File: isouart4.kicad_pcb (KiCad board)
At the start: 2 copper layers, 89 x 99 mm, 83 parts, among them J1 USB_B, J2 Conn_01x04, J3 Conn_01x04, J4 Conn_01x04, J5 Conn_01x04, U1 AMS1117-3.3, U10 74HC123, U11 74HC123, U2 π122U31, U3 π122U31, U4 π122U31, U5 π122U31, U7 CH344Q, U8 74HC123, U9 74HC123, Y1 8MHz

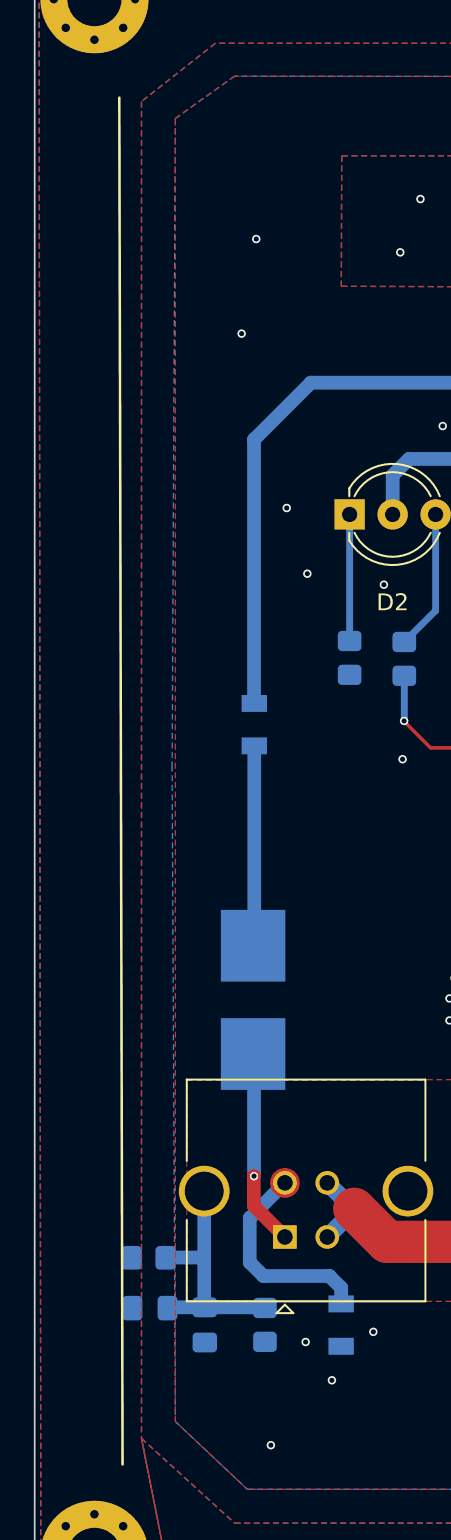
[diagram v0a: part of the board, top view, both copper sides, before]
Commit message: Adjust R1, C1 and C10 poisitions
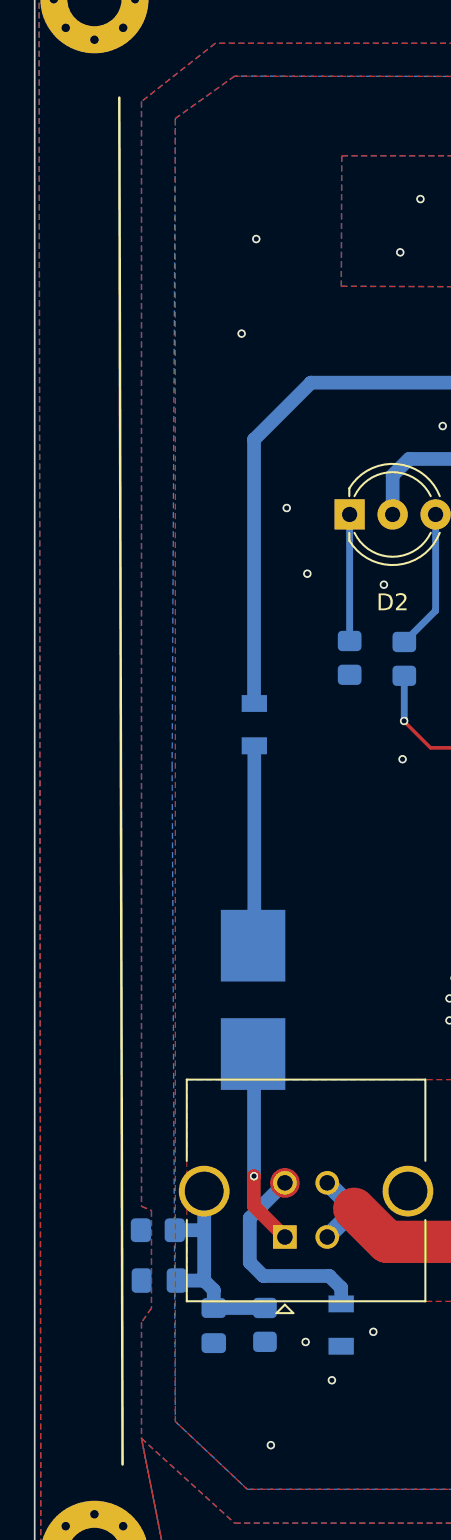
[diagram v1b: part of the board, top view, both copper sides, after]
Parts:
- moved R1 1.72 mm to (147.0, 115.7)
- moved C3 1.72 mm to (147.0, 118.7)
- moved C10 0.53 mm to (150.3, 121.3)
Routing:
- net /USBSHLD: track 14.9 -> 13.6 mm
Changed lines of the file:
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@@
   )
   (footprint "Resistor_SMD:R_0805_2012Metric_Pad1.20x1.40mm_HandSolder" (layer "B.Cu")
-    (at 146.425 117.325)
+    (at 146.965 115.695)
     (descr "Resistor SMD 0805 (2012 Metric), square (rectangular) end terminal, IPC_7351 nominal with elongated pad for handsoldering. (Body size source: IPC-SM-782 page 72, https://www.pcb-3d.com/wordpress/wp-content/uploads/ipc-sm-782a_amendment_1_and_2.pdf), generated with kicad-footprint-generator")
     (tags "resistor handsolder")
@@
   )
   (footprint "Capacitor_SMD:C_0805_2012Metric_Pad1.18x1.45mm_HandSolder" (layer "B.Cu")
-    (at 146.5 120.3)
+    (at 147.04 118.67)
     (descr "Capacitor SMD 0805 (2012 Metric), square (rectangular) end terminal, IPC_7351 nominal with elongated pad for handsoldering. (Body size source: IPC-SM-782 page 76, https://www.pcb-3d.com/wordpress/wp-content/uploads/ipc-sm-782a_amendment_1_and_2.pdf, https://docs.google.com/spreadsheets/d/1BsfQQcO9C6DZCsRaXUlFlo91Tg2WpOkGARC1WS5S8t0/edit?usp=sharing), generated with kicad-footprint-generator")
     (tags "capacitor handsolder")
@@
   )
   (footprint "Capacitor_SMD:C_0805_2012Metric_Pad1.18x1.45mm_HandSolder" (layer "B.Cu")
-    (at 149.74 121.29 90)
+    (at 150.27 121.33 90)
     (descr "Capacitor SMD 0805 (2012 Metric), square (rectangular) end terminal, IPC_7351 nominal with elongated pad for handsoldering. (Body size source: IPC-SM-782 page 76, https://www.pcb-3d.com/wordpress/wp-content/uploads/ipc-sm-782a_amendment_1_and_2.pdf, https://docs.google.com/spreadsheets/d/1BsfQQcO9C6DZCsRaXUlFlo91Tg2WpOkGARC1WS5S8t0/edit?usp=sharing), generated with kicad-footprint-generator")
     (tags "capacitor handsolder")
@@
   (segment (start 170.01 110.015) (end 173.665559 106.359441) (width 0.254) (layer "B.Cu") (net 6))
   (segment (start 173.665559 103.543629) (end 173.665559 102.951687) (width 0.254) (layer "B.Cu") (net 6))
-  (segment (start 147.44 117.31) (end 149.70505 117.31) (width 0.8128) (layer "B.Cu") (net 7))
-  (segment (start 149.70505 113.38485) (end 149.70505 117.31) (width 0.8128) (layer "B.Cu") (net 7))
+  (segment (start 149.70505 113.38485) (end 149.70505 115.7) (width 0.8128) (layer "B.Cu") (net 7))
   (segment (start 149.70505 120.21755) (end 149.74 120.2525) (width 0.2) (layer "B.Cu") (net 7))
   (segment (start 153.2585 120.2525) (end 153.296 120.29) (width 0.8128) (layer "B.Cu") (net 7))
-  (segment (start 149.70505 117.31) (end 149.70505 120.21755) (width 0.8128) (layer "B.Cu") (net 7))
-  (segment (start 149.74 120.2525) (end 153.2585 120.2525) (width 0.8128) (layer "B.Cu") (net 7))
-  (segment (start 147.425 117.325) (end 147.44 117.31) (width 0.8128) (layer "B.Cu") (net 7))
-  (segment (start 149.74 120.2525) (end 147.5525 120.2525) (width 0.8128) (layer "B.Cu") (net 7))
+  (segment (start 148.0775 118.67) (end 149.70505 118.67) (width 0.8128) (layer "B.Cu") (net 7))
+  (segment (start 147.965 115.695) (end 149.70005 115.695) (width 0.8128) (layer "B.Cu") (net 7))
+  (segment (start 153.2935 120.2925) (end 153.296 120.29) (width 0.2) (layer "B.Cu") (net 7))
+  (segment (start 150.27 119.23495) (end 149.70505 118.67) (width 0.8128) (layer "B.Cu") (net 7))
+  (segment (start 150.27 120.2925) (end 153.2935 120.2925) (width 0.8128) (layer "B.Cu") (net 7))
+  (segment (start 150.27 120.2925) (end 150.27 119.23495) (width 0.8128) (layer "B.Cu") (net 7))
+  (segment (start 149.70505 115.7) (end 149.70505 118.67) (width 0.8128) (layer "B.Cu") (net 7))
   (segment (start 152.65 84.555) (end 152.665 84.57) (width 0.8128) (layer "B.Cu") (net 8))
   (segment (start 152.65 68.975) (end 152.65 84.555) (width 0.8128) (layer "B.Cu") (net 8))
@@
         (xy 150.36 45.56)
         (xy 146 49)
+        (xy 146 114.28)
+        (xy 146.59 114.53)
+        (xy 146.59 120.3)
+        (xy 146 121.14)
         (xy 146 128)
         (xy 148 138.1)

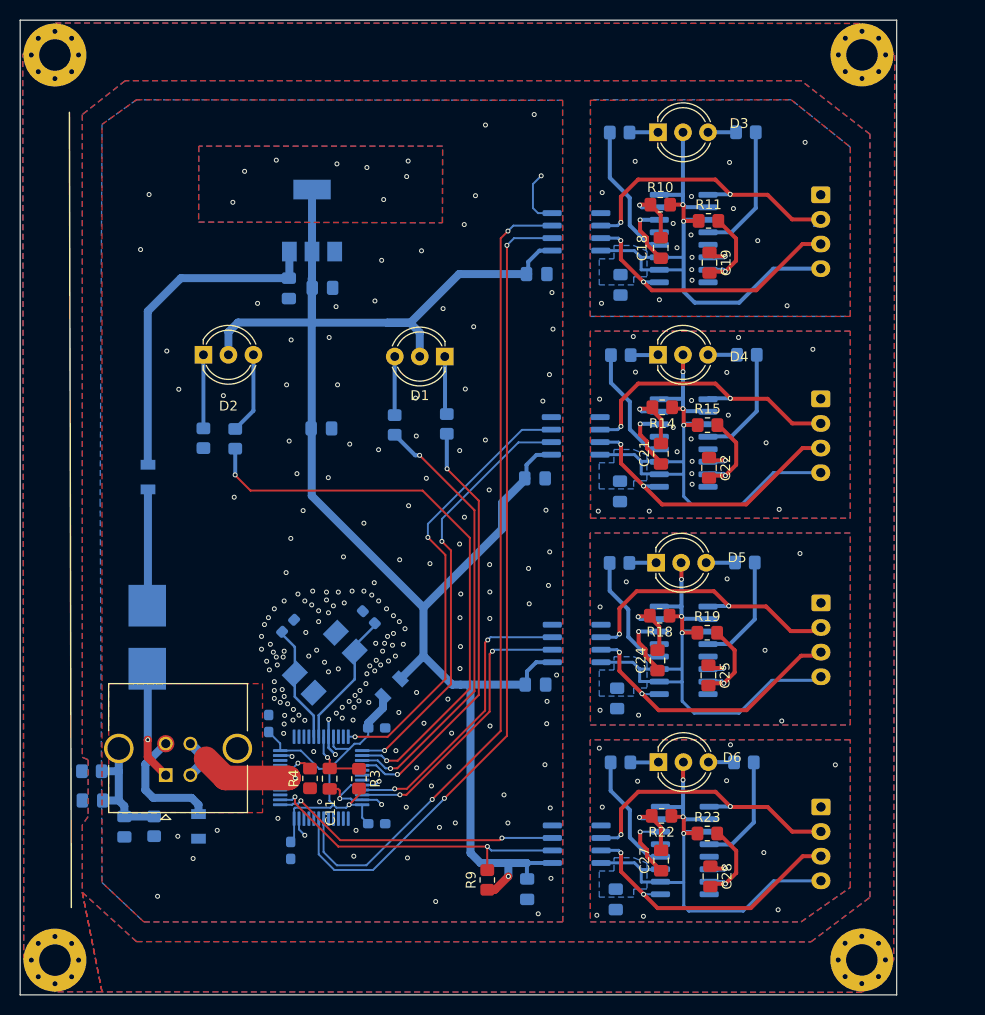
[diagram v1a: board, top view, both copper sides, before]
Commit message: pcb: adjust mounting hole positions; SHLD outer line at 0.4mm from edge
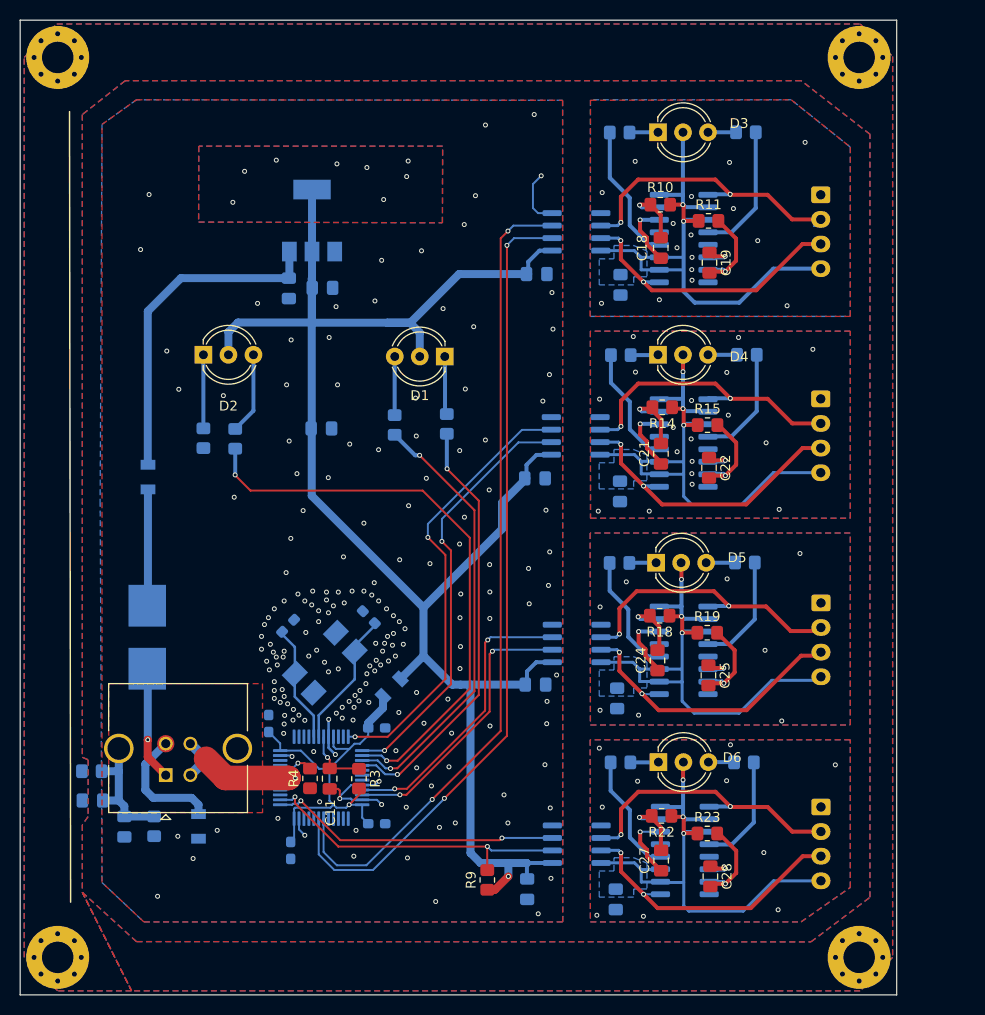
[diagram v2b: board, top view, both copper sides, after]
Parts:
- moved H1 0.39 mm to (143.5, 134.6)
- moved H2 0.39 mm to (224.9, 43.2)
- moved H4 0.38 mm to (143.5, 43.2)
- moved H3 0.37 mm to (224.9, 134.6)
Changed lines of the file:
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@@
   (net 108 "/SHLD")
   (footprint "MountingHole:MountingHole_3.2mm_M3_Pad_Via" (layer "F.Cu")
-    (at 143.22 134.88)
+    (at 143.497056 134.602944)
     (descr "Mounting Hole 3.2mm, M3")
     (tags "mounting hole 3.2mm m3")
@@
   )
   (footprint "MountingHole:MountingHole_3.2mm_M3_Pad_Via" (layer "F.Cu")
-    (at 225.17 134.86)
+    (at 224.9 134.6)
     (descr "Mounting Hole 3.2mm, M3")
     (tags "mounting hole 3.2mm m3")
@@
   )
   (footprint "MountingHole:MountingHole_3.2mm_M3_Pad_Via" (layer "F.Cu")
-    (at 143.22 42.95)
+    (at 143.5 43.2)
     (descr "Mounting Hole 3.2mm, M3")
     (tags "mounting hole 3.2mm m3")
@@
   )
   (footprint "MountingHole:MountingHole_3.2mm_M3_Pad_Via" (layer "F.Cu")
-    (at 225.19 42.94)
+    (at 224.9 43.2)
     (descr "Mounting Hole 3.2mm, M3")
     (tags "mounting hole 3.2mm m3")
@@
     )
   )
-  (gr_line (start 144.8816 129.54) (end 144.689 48.768)
+  (gr_line (start 144.811 129) (end 144.7 48.7)
     (stroke (width 0.15) (type default)) (layer "F.SilkS"))
   (gr_line (start 134.366 73.406) (end 230.759 73.406)
@@
     (stroke (width 0.1) (type default)) (fill none) (layer "Edge.Cuts"))
   (dimension (type aligned) (layer "Dwgs.User")
+    (pts (xy 224.9 43.2) (xy 224.9 134.6))
+    (height -8.1)
+    (gr_text "91.4000 mm" (at 231.85 88.9 90) (layer "Dwgs.User")
+      (effects (font (size 1 1) (thickness 0.15)))
+    )
+    (format (prefix "") (suffix "") (units 3) (units_format 1) (precision 4))
+    (style (thickness 0.15) (arrow_length 1.27) (text_position_mode 0) (extension_height 0.58642) (extension_offset 0.5) keep_text_aligned)
+  )
+  (dimension (type aligned) (layer "Dwgs.User")
     (pts (xy 133.578433 138.43) (xy 133.578433 119.38))
     (height -4.038433)
@@
   )
   (dimension (type aligned) (layer "Dwgs.User")
+    (pts (xy 143.5 43.2) (xy 224.9 43.2))
+    (height -7.7)
+    (gr_text "81.4000 mm" (at 184.2 34.35) (layer "Dwgs.User")
+      (effects (font (size 1 1) (thickness 0.15)))
+    )
+    (format (prefix "") (suffix "") (units 3) (units_format 1) (precision 4))
+    (style (thickness 0.15) (arrow_length 1.27) (text_position_mode 0) (extension_height 0.58642) (extension_offset 0.5) keep_text_aligned)
+  )
+  (dimension (type aligned) (layer "Dwgs.User")
     (pts (xy 129.54 141.153) (xy 139.62 141.153))
     (height 3.5)
@@
     (polygon
       (pts
-        (xy 225.208895 39.747062)
-        (xy 228.508895 42.947062)
-        (xy 228.408895 134.897062)
-        (xy 225.208895 138.147062)
-        (xy 221.258895 138.147062)
-        (xy 148 138.1)
+        (xy 225 39.8)
+        (xy 228.3 43.1)
+        (xy 228.3 134.6)
+        (xy 225 138)
+        (xy 151 138)
         (xy 146 128)
         (xy 151.5 133)
@@
         (xy 146 121.14)
         (xy 146 128)
-        (xy 148 138.1)
-        (xy 143.25 138.1)
-        (xy 140.05 134.85)
-        (xy 139.95 42.9)
-        (xy 143.25 39.7)
-        (xy 147.3 39.7)
+        (xy 151 138)
+        (xy 143.5 138)
+        (xy 140.1 134.6)
+        (xy 140.1 43.2)
+        (xy 143.4 39.8)
       )
     )

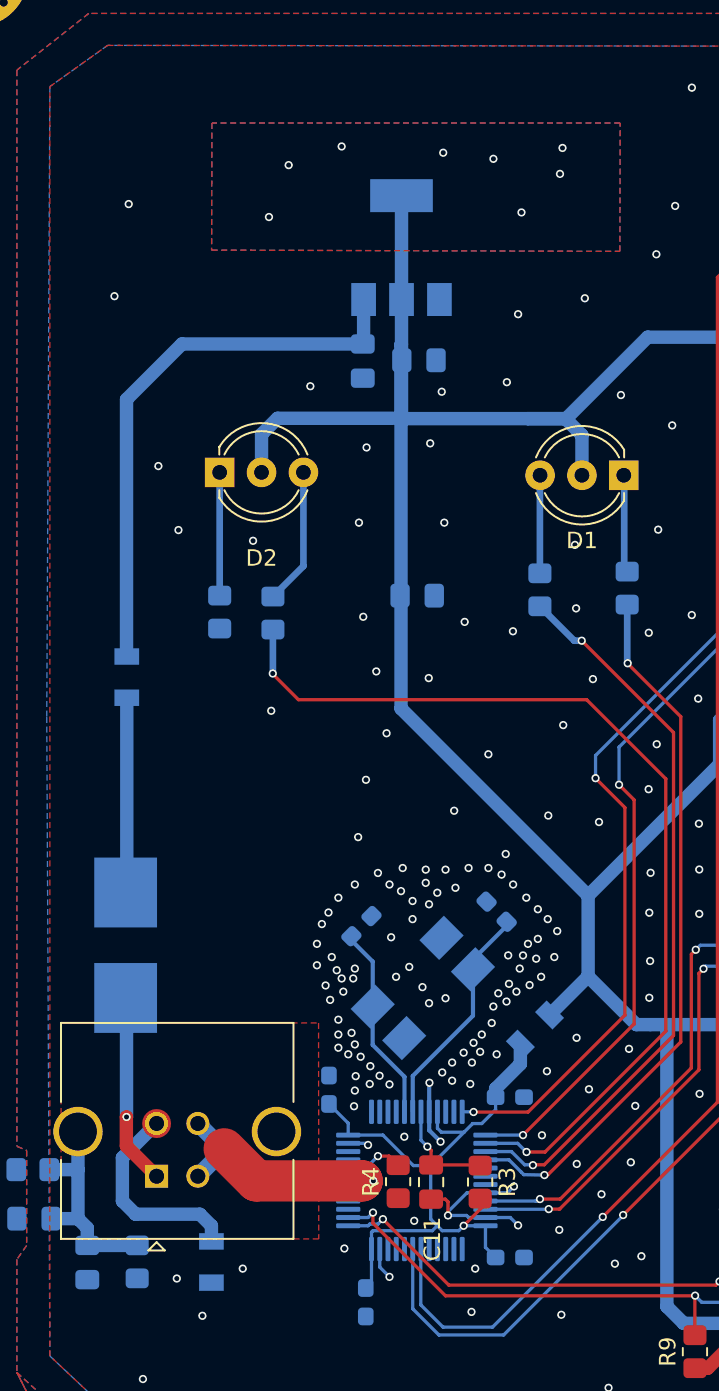
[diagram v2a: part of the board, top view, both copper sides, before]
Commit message: adjust power filtering
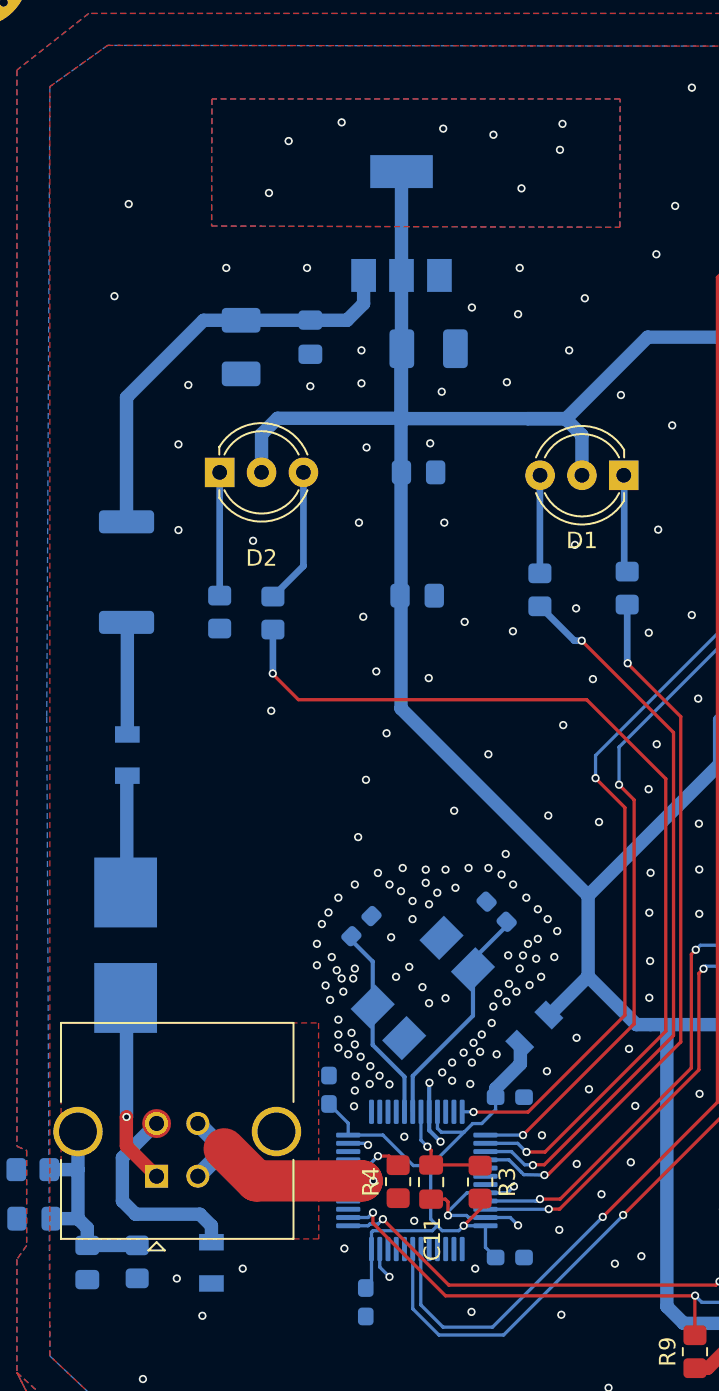
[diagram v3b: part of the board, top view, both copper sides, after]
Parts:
- removed L1, L2, L3: L_Ferrite_Small, isouart4:FB_0805_2012Metric
- added C30: 100n, Capacitor_SMD:C_0805_2012Metric_Pad1.18x1.45mm_HandSolder, B.Cu at (163.8, 65.2)
- added C31: 100n, Capacitor_SMD:C_0805_2012Metric_Pad1.18x1.45mm_HandSolder, B.Cu at (170.4, 73.4)
- added FB1: 100R, isouart4:FB_0805_2012Metric, B.Cu at (152.7, 90.5)
- added FB2: 100R, isouart4:FB_0805_2012Metric, B.Cu at (157.8, 121.3)
- added FB3: 100R, isouart4:FB_0805_2012Metric, B.Cu at (177.4, 107.2)
- added R26: 4R3, Resistor_SMD:R_2512_6332Metric_Pad1.40x3.35mm_HandSolder, B.Cu at (152.7, 79.5)
- C1: footprint Capacitor_SMD:C_0805_2012Metric_Pad1.18x1.45mm_HandSolder -> Capacitor_Tantalum_SMD:CP_EIA-3528-15_AVX-H_Pad1.50x2.35mm_HandSolder
- C2: value 10uF -> 22uF; footprint Capacitor_SMD:C_0805_2012Metric_Pad1.18x1.45mm_HandSolder -> Capacitor_Tantalum_SMD:CP_EIA-3528-15_AVX-H_Pad1.50x2.35mm_HandSolder
- moved C1 7.43 mm to (159.6, 65.8)
- moved U1 1.46 mm to (169.3, 58.3)
- moved C2 0.91 mm to (171.0, 65.9)
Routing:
- net Net-(U1-VI): track 34.2 -> 26.0 mm
- net Net-(FB1-Pad1): track 0.00 -> 6.82 mm
- net Net-(F1-Pad2): track 11.8 -> 7.13 mm
- net /USB-UART4-CH344Q/VIN 3.3V: track 174.0 -> 175.4 mm
- net GND: vias 181 -> 189
